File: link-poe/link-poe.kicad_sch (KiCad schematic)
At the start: 26 parts, among them J101 2x05_Horizontal, J102 NE8FAH, J103 DX07S016JA3, J104 2x05_Horizontal, J105 NE8FAH, J106 WAGO 2065-100, J107 WAGO 2065-100, J108 WAGO 2065-100, J109 WAGO 2065-100

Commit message: Use date as revision
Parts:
- ICON104: value 24V -> 28V; footprint V2_Artwork:24V -> V2_Artwork:28V; symbol V2_Artwork:24V -> V2_Artwork:28V
- TVS101: value SMBJ36CA -> SMBJ33CA; symbol V2_Diode:SMBJ36CA -> V2_Diode:SMBJ33CA; Mouser 652-SMBJ36CA-Q -> 652-SMBJ33CA-Q; Product SMBJ36CA-Q -> SMBJ33CA-Q; Rating 36V -> 33V
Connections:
- net +24V renamed +28V

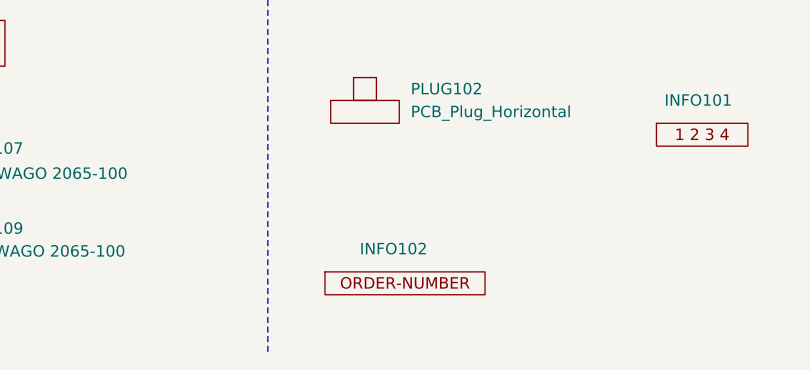
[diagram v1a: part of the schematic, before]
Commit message: Replace Order_Number
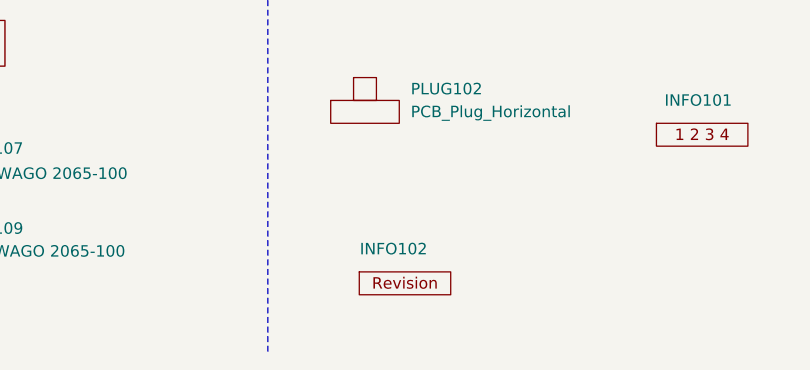
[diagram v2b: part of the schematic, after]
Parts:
- ICON104: value 28V -> ~
- INFO102: value Order_Number -> ~; footprint V2_Production:Order_Number -> V2_Production:Revision; symbol V2_Production:Order_Number -> V2_Production:Revision
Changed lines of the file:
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@@
 	)
 	(symbol
-		(lib_id "V2_Production:Order_Number")
+		(lib_id "V2_Production:Revision")
 		(at 191.77 189.23 0)
 		(unit 1)
@@
 			)
 		)
-		(property "Value" "Order_Number"
+		(property "Value" "~"
 			(at 191.77 191.77 0)
 			(effects
@@
 			)
 		)
-		(property "Footprint" "V2_Production:Order_Number"
+		(property "Footprint" "V2_Production:Revision"
 			(at 191.77 194.31 0)
 			(effects
@@
 			)
 		)
-		(property "Value" "28V"
+		(property "Value" "~"
 			(at 243.84 172.72 0)
 			(effects
@@
 			(at 224.79 153.67 0)
 			(effects
-				(font
-					(size 1.27 1.27)
-				)
-				(hide yes)
-			)
-		)
-		(property "Sim.Enable" "0"
-			(at 224.79 153.67 0)
-			(effects

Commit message: Update Library
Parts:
- R101, R102: symbol V2_Device:R_0603_5k1 -> V2_Resistor:0603_5k1

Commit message: Refresh
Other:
- note added: "PoE Passive +28V IEEE 802.3af Mode B"
- note removed: "PoE Passive +24V IEEE 802.3af Mode B"
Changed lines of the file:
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@@
 		)
 	)
-	(text "PoE Passive +24V\nIEEE 802.3af Mode B"
+	(text "PoE Passive +28V\nIEEE 802.3af Mode B"
 		(exclude_from_sim no)
 		(at 46.99 113.03 0)
@@
 		(at 187.325 168.91 0)
 		(unit 1)
-		(exclude_from_sim no)
+		(exclude_from_sim yes)
 		(in_bom no)
 		(on_board yes)
@@
 			)
 		)
-		(property "Sim.Enable" "0"
-			(at 187.325 168.91 0)
-			(effects
-				(font
-					(size 1.27 1.27)
-				)
-				(hide yes)
-			)
-		)
 		(instances
 			(project "power-rj45"
@@
 		(at 187.325 152.4 0)
 		(unit 1)
-		(exclude_from_sim no)
+		(exclude_from_sim yes)
 		(in_bom no)
 		(on_board yes)
@@
 			)
 		)
-		(property "Sim.Enable" "0"
-			(at 187.325 152.4 0)
-			(effects
-				(font
-					(size 1.27 1.27)
-				)
-				(hide yes)
-			)
-		)
 		(instances
 			(project "power-rj45"
@@
 		(at 242.57 154.94 0)
 		(unit 1)
-		(exclude_from_sim no)
+		(exclude_from_sim yes)
 		(in_bom no)
 		(on_board yes)
@@
 			)
 		)
-		(property "Sim.Enable" "0"
-			(at 242.57 154.94 0)
-			(effects
-				(font
-					(size 1.27 1.27)
-				)
-				(hide yes)
-			)
-		)
 		(instances
 			(project "power-rj45"
@@
 		(at 267.97 172.72 0)
 		(unit 1)
-		(exclude_from_sim no)
+		(exclude_from_sim yes)
 		(in_bom no)
 		(on_board yes)
@@
 			)
 		)
-		(property "Sim.Enable" "0"
-			(at 267.97 172.72 0)
-			(effects
-				(font
-					(size 1.27 1.27)
-				)
-				(hide yes)
-			)
-		)
 		(instances
 			(project ""
@@
 		(at 242.57 149.86 0)
 		(unit 1)
-		(exclude_from_sim no)
+		(exclude_from_sim yes)
 		(in_bom no)
 		(on_board yes)
@@
 			)
 		)
-		(property "Sim.Enable" "0"
-			(at 242.57 149.86 0)
-			(effects
-				(font
-					(size 1.27 1.27)
-				)
-				(hide yes)
-			)
-		)
 		(instances
 			(project "power-rj45"
@@
 		(at 243.84 172.72 0)
 		(unit 1)
-		(exclude_from_sim no)
+		(exclude_from_sim yes)
 		(in_bom no)
 		(on_board yes)
@@
 			)
 		)
-		(property "Sim.Enable" "0"
-			(at 243.84 172.72 0)
-			(effects
-				(font
-					(size 1.27 1.27)
-				)
-				(hide yes)
-			)
-		)
 		(instances
 			(project "power-rj45"
@@
 		(at 267.97 167.64 0)
 		(unit 1)
-		(exclude_from_sim no)
+		(exclude_from_sim yes)
 		(in_bom no)
 		(on_board yes)
@@
 			(at 267.97 167.64 0)
 			(effects
-				(font
-					(size 1.27 1.27)
-				)
-				(hide yes)
-			)
-		)
-		(property "Sim.Enable" "0"
-			(at 267.97 167.64 0)
-			(effects

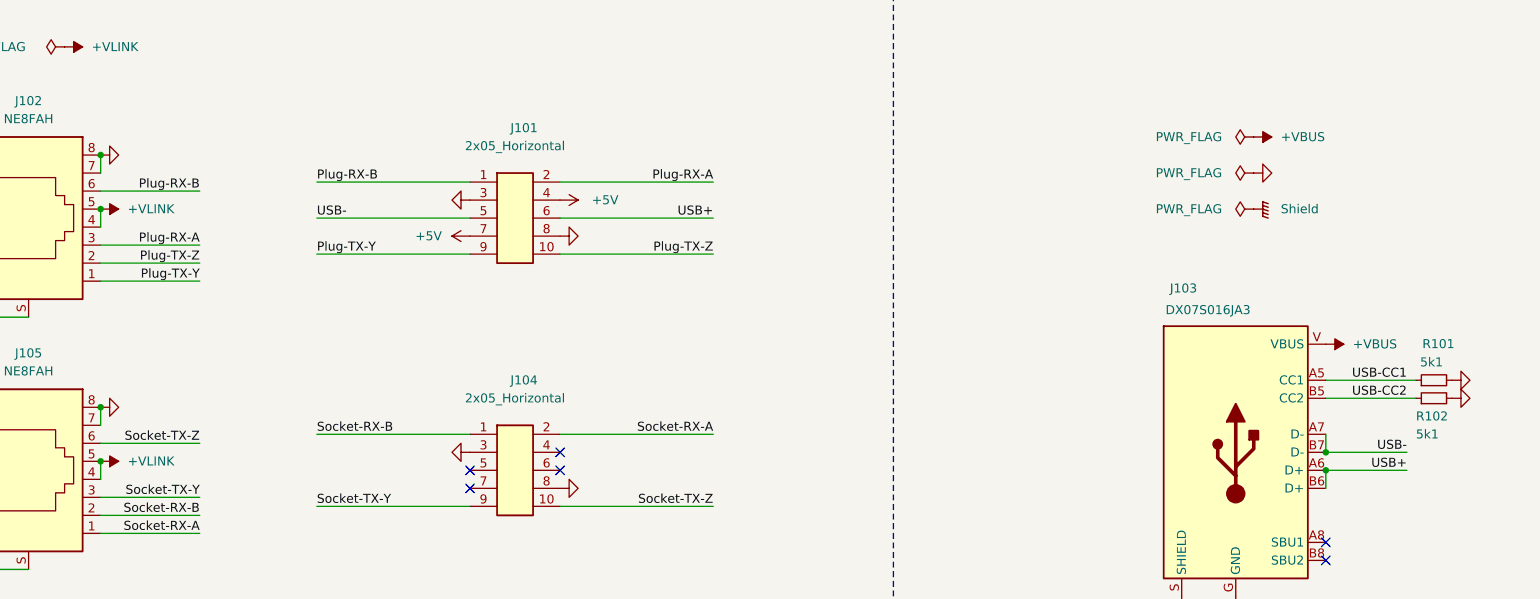
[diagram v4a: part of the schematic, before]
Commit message: Replace step-down
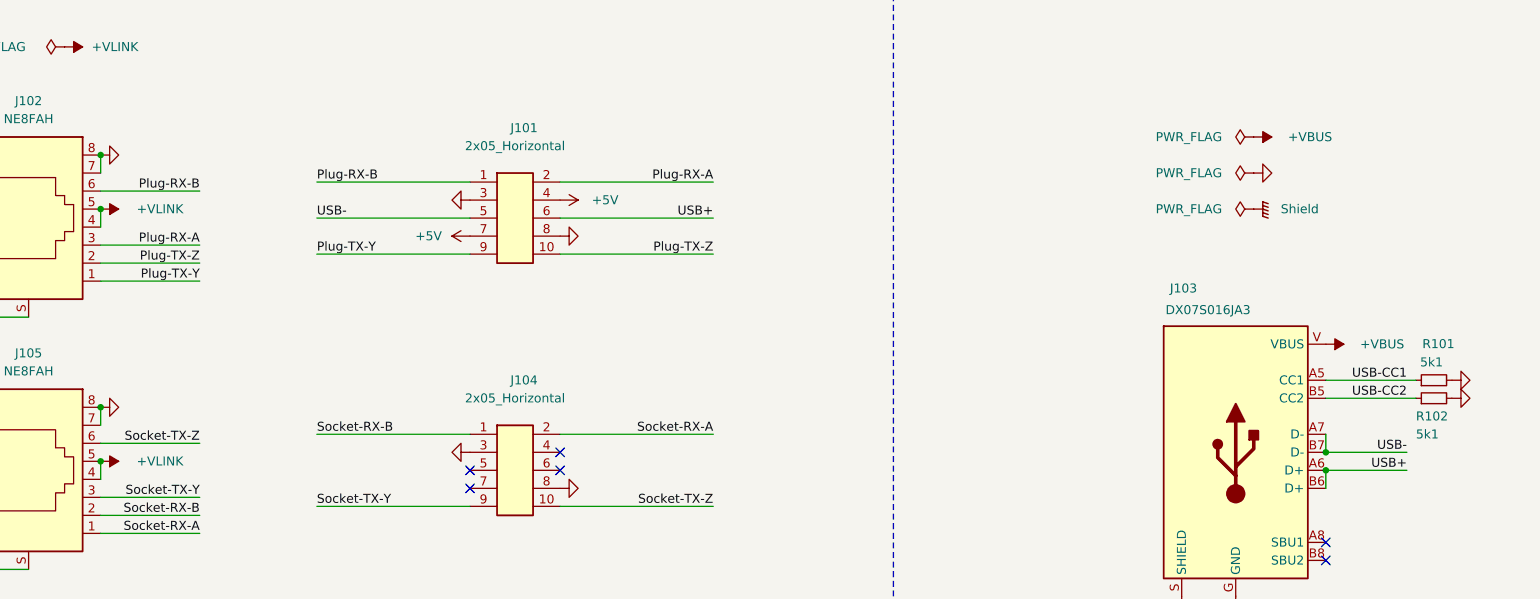
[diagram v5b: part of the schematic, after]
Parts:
- ICON104, INFO102: value ~ -> (none)

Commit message: Update
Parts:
- J101: renamed from J102; Id (none) -> EtherCon:${SYMBOL_NAME}; Rating (none) -> CAT5e
- J102: renamed from J105; Id (none) -> EtherCon:${SYMBOL_NAME}; Rating (none) -> CAT5e
- J103: renamed from J106; Id (none) -> WAGO:${SYMBOL_NAME}; Rating (none) -> 9A
- J104: renamed from J108; Id (none) -> WAGO:${SYMBOL_NAME}; Rating (none) -> 9A
- J105: renamed from J101; Id (none) -> Header:${SYMBOL_NAME}; Rating (none) -> 1A
- J106: renamed from J104; Id (none) -> Header:${SYMBOL_NAME}; Rating (none) -> 1A
- J107: Id (none) -> WAGO:${SYMBOL_NAME}; Rating (none) -> 9A
- J108: renamed from J109; Id (none) -> WAGO:${SYMBOL_NAME}; Rating (none) -> 9A
- J109: renamed from J103; Id (none) -> USB:${SYMBOL_NAME}; Rating (none) -> USB2.0
- R101, R102: Id (none) -> Resistor:${SYMBOL_NAME}
- TVS101: Id (none) -> Diode:${SYMBOL_NAME}
- renumbered ICON102 to ICON101, ICON101 to ICON102, ICON106 to ICON105, ICON105 to ICON106, INFO102 to INFO101, INFO101 to INFO102

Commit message: Good Bye Imperial
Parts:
- R101, R102: footprint V2_Resistor_SMD:R_0603 -> V2_Resistor_SMD:R_1608; symbol V2_Resistor:0603_5k1 -> V2_Resistor:1608_5k1
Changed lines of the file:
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@@
 	)
 	(symbol
-		(lib_id "V2_Resistor:0603_5k1")
+		(lib_id "V2_Resistor:1608_5k1")
 		(at 252.73 72.39 90)
 		(unit 1)
@@
 			)
 		)
-		(property "Footprint" "V2_Resistor_SMD:R_0603"
+		(property "Footprint" "V2_Resistor_SMD:R_1608"
 			(at 268.478 72.39 0)
 			(hide yes)
@@
 	)
 	(symbol
-		(lib_id "V2_Resistor:0603_5k1")
+		(lib_id "V2_Resistor:1608_5k1")
 		(at 252.73 74.93 90)
 		(unit 1)
@@
 			)
 		)
-		(property "Footprint" "V2_Resistor_SMD:R_0603"
+		(property "Footprint" "V2_Resistor_SMD:R_1608"
 			(at 268.478 74.93 0)
 			(hide yes)

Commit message: Refresh
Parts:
- INFO102: value Layer_Numbers -> Layer_Numbers-4; footprint V2_Production:Layer_Numbers -> V2_Production:Layer_Numbers-4; symbol V2_Production:Layer_Numbers -> V2_Production:Layer_Numbers-4
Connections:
- net +VBUS: no longer names the net of J109.V (VBUS)
- no-connect marks 6 -> 7
